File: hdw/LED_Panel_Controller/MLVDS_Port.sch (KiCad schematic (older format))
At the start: 4 parts

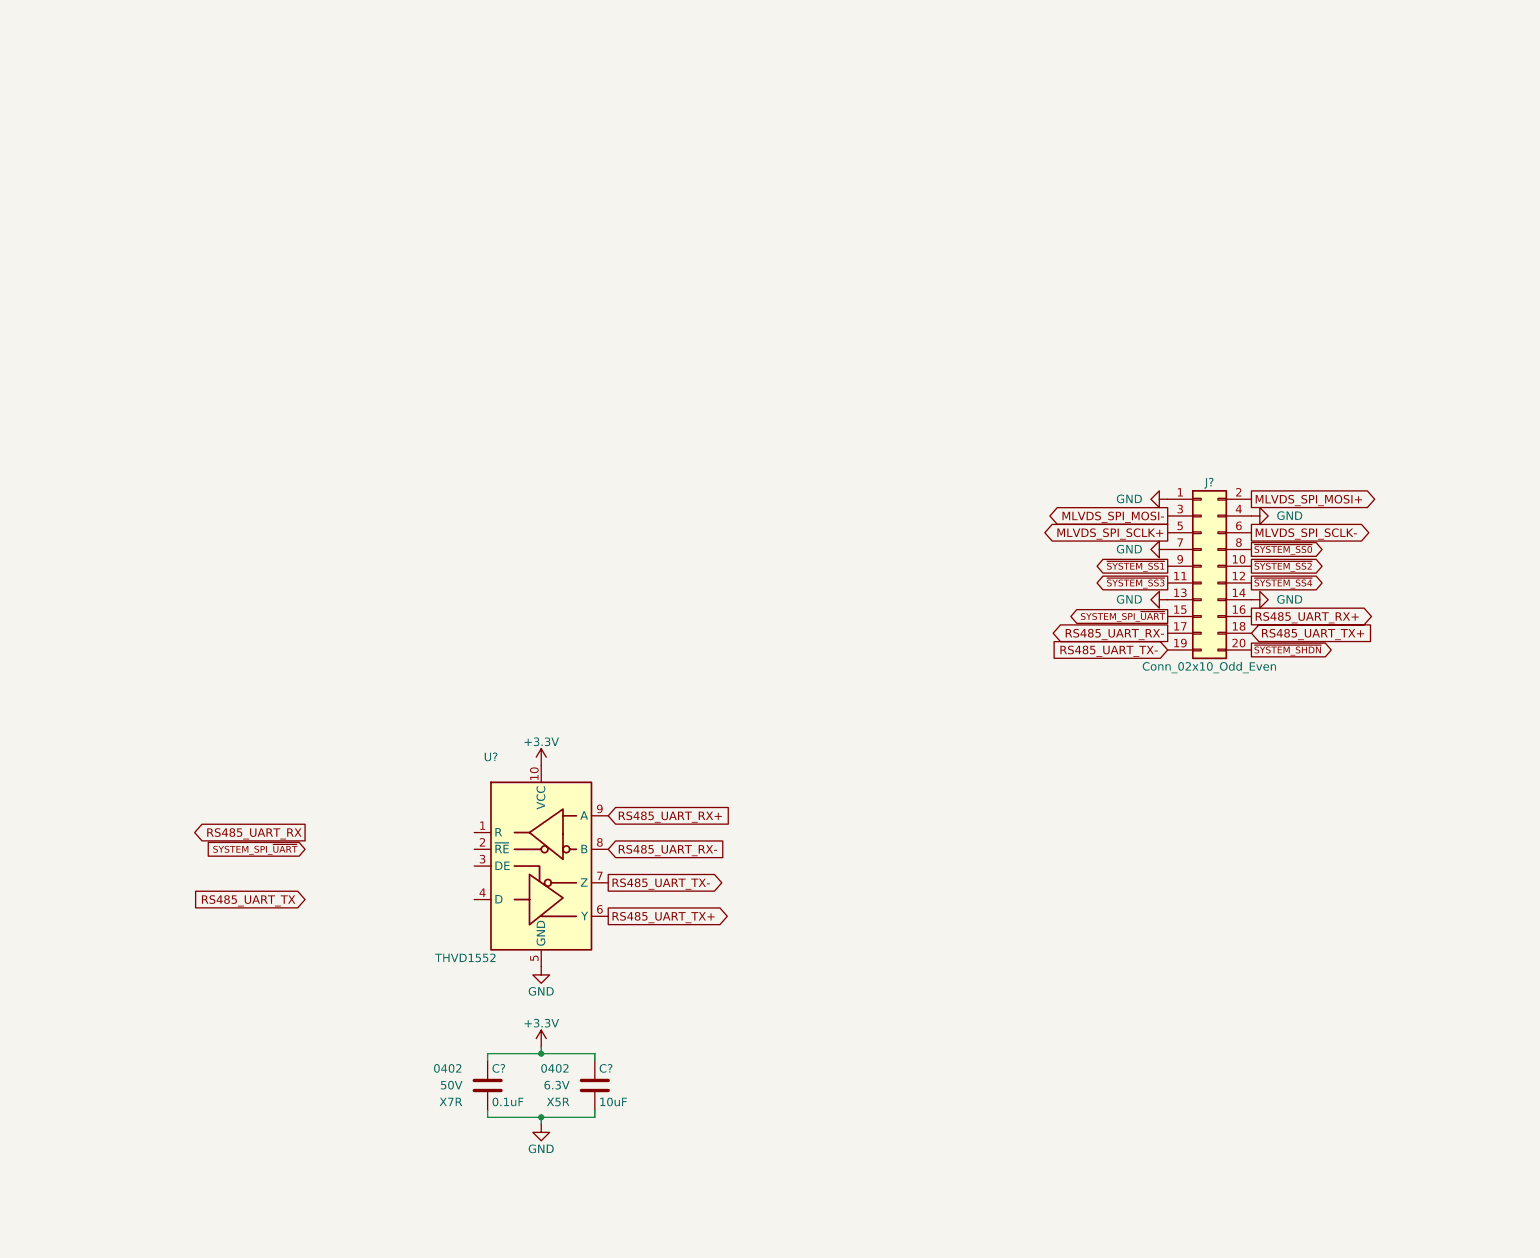
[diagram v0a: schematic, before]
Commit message: reworked schematic to use MLVDS connector instead of wifi module
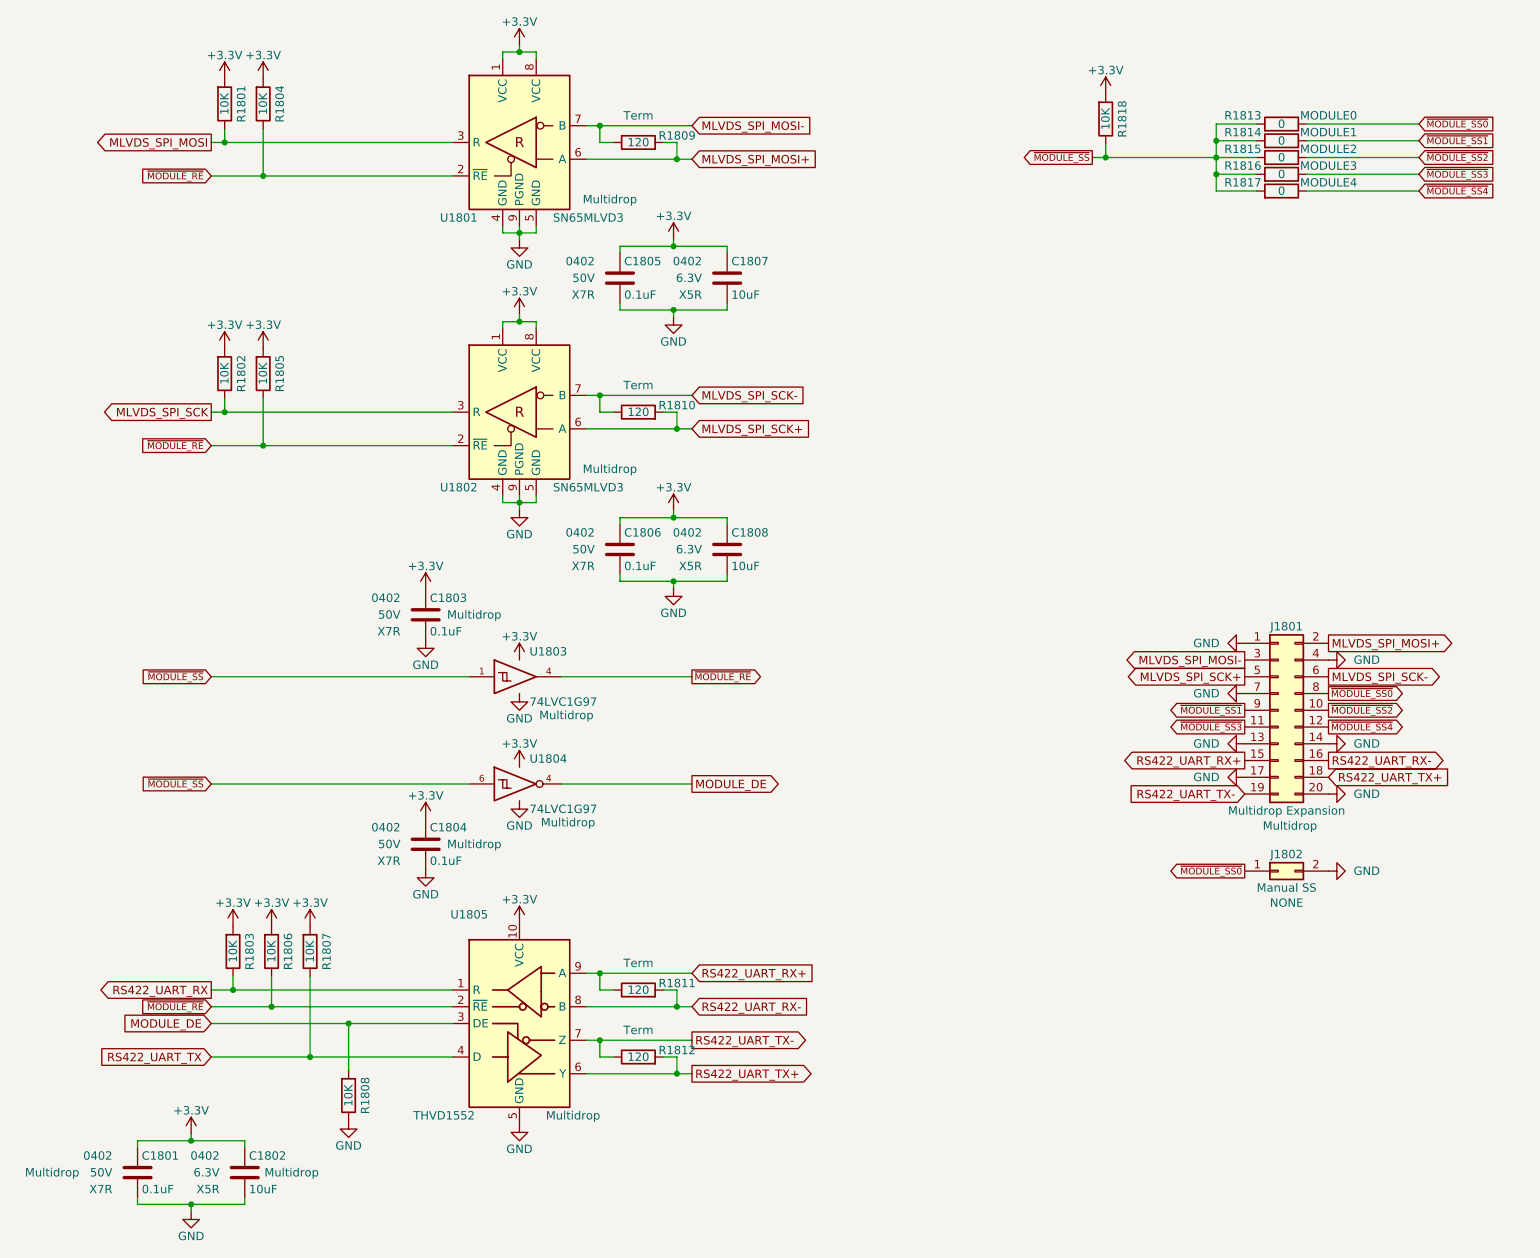
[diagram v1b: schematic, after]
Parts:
- added C1803, C1804, C1805, C1806: 0.1uF, Capacitors_SMD:C_0402, symbol Custom_Library:C_Custom
- added C1807, C1808: 10uF, Capacitors_SMD:C_0402, symbol Custom_Library:C_Custom
- added J1802: Manual SS, symbol Connector_Generic:Conn_02x01
- added R1801, R1802, R1803, R1804, R1805, R1806, R1807, R1808, R1818: 10K, Resistors_SMD:R_0402, symbol Custom_Library:R_Custom
- added R1809, R1810, R1811, R1812: 120, Resistors_SMD:R_0402, symbol Custom_Library:R_Custom
- added R1813, R1814, R1815, R1816, R1817: 0, Resistors_SMD:R_0402, symbol Custom_Library:R_Custom
- added U1801, U1802: SN65MLVD3, Housings_DFN_QFN:DFN-8-1EP_3x3mm_Pitch0.65mm, symbol Custom_Library:SN65MLVD3
- added U1803: 74LVC1G97, Package_TO_SOT_SMD:SOT-363_SC-70-6, symbol Custom_Library:74LVC1G97_Power_BUF
- added U1804: 74LVC1G97, Package_TO_SOT_SMD:SOT-363_SC-70-6, symbol Custom_Library:74LVC1G97_Power_NOT
- C1801, C1802: renamed from C?; Configuration (none) -> Multidrop
- J1801: renamed from J?; value Conn_02x10_Odd_Even -> Multidrop Expansion; footprint (none) -> Connector_IDC:IDC-Header_2x10_P2.54mm_Vertical; Configuration (none) -> Multidrop
- U1805: renamed from U?; Configuration (none) -> Multidrop
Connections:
- net SYSTEM_SPI_~UART is gone; now on net RS422_UART_RX+: J1801.15 (Pin_15)
- net ~SYSTEM_SHDN is gone; now on net GND: J1801.20 (Pin_20)
- net +3V3: now also C1803.1, C1804.1, C1805.1, C1806.1, C1807.1, C1808.1, R1801.1, R1802.1, R1803.1, R1804.1, R1805.1, R1806.1, R1807.1, R1818.1, U1801.1 (VCC), U1801.8 (VCC), U1802.1 (VCC), U1802.8 (VCC), U1803.5 (VCC), U1804.1 (VCC), U1804.5 (VCC)
- net GND: now also J1801.17 (Pin_17), C1803.2, C1804.2, C1805.2, C1806.2, C1807.2, C1808.2, J1802.2 (Pin_2), R1808.2, U1801.4 (GND), U1801.5 (GND), U1801.9 (PGND), U1802.4 (GND), U1802.5 (GND), U1802.9 (PGND), U1803.2 (GND), U1803.3 (GND), U1803.6 (GND), U1804.2 (GND), U1804.3 (GND)
- net MLVDS_SPI_MOSI+: now also R1809.1, U1801.6 (A)
- net MLVDS_SPI_MOSI-: now also R1809.2, U1801.7 (B)
- net RS422_UART_RX: now reaches U1805.1 (R)
- net RS422_UART_RX: now also R1803.2
- net ~MODULE_RE: now reaches U1805.2 (~RE)
- net ~MODULE_RE: now also R1804.2, R1805.2, R1806.2, U1801.2 (~RE), U1802.2 (~RE), U1803.4
- net MODULE_DE: now reaches U1805.3 (DE)
- net MODULE_DE: now also R1808.1, U1804.4
- net RS422_UART_TX: now reaches U1805.4 (D)
- net RS422_UART_TX: now also R1807.2
- net MLVDS_SPI_SCLK+ renamed MLVDS_SPI_SCK+
- net MLVDS_SPI_SCK+: now also R1810.1, U1802.6 (A)
- net MLVDS_SPI_SCLK- renamed MLVDS_SPI_SCK-
- net MLVDS_SPI_SCK-: now also R1810.2, U1802.7 (B)
- net RS485_UART_RX+ renamed RS422_UART_RX+
- net RS422_UART_RX+: now also R1811.2; no longer J1801.16 (Pin_16)
- net RS485_UART_RX- renamed RS422_UART_RX-
- net RS422_UART_RX-: now also J1801.16 (Pin_16), R1811.1; no longer J1801.17 (Pin_17)
- net RS485_UART_TX+ renamed RS422_UART_TX+
- net RS422_UART_TX+: now also R1812.1
- net RS485_UART_TX- renamed RS422_UART_TX-
- net RS422_UART_TX-: now also R1812.2
- net ~SYSTEM_SS0 renamed ~MODULE_SS0
- net ~MODULE_SS0: now also J1802.1 (Pin_1), R1813.2
- net ~SYSTEM_SS1 renamed ~MODULE_SS1
- net ~MODULE_SS1: now also R1814.2
- net ~SYSTEM_SS2 renamed ~MODULE_SS2
- net ~MODULE_SS2: now also R1815.2
- net ~SYSTEM_SS3 renamed ~MODULE_SS3
- net ~MODULE_SS3: now also R1816.2
- net ~SYSTEM_SS4 renamed ~MODULE_SS4
- net ~MODULE_SS4: now also R1817.2
- new net MLVDS_SPI_MOSI: R1801.2, U1801.3 (R)
- new net MLVDS_SPI_SCK: R1802.2, U1802.3 (R)
- new net ~MODULE_SS: R1813.1, R1814.1, R1815.1, R1816.1, R1817.1, R1818.2, U1803.1, U1804.6
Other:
- moved on the sheet: C1801, C1802, J1801, U1805

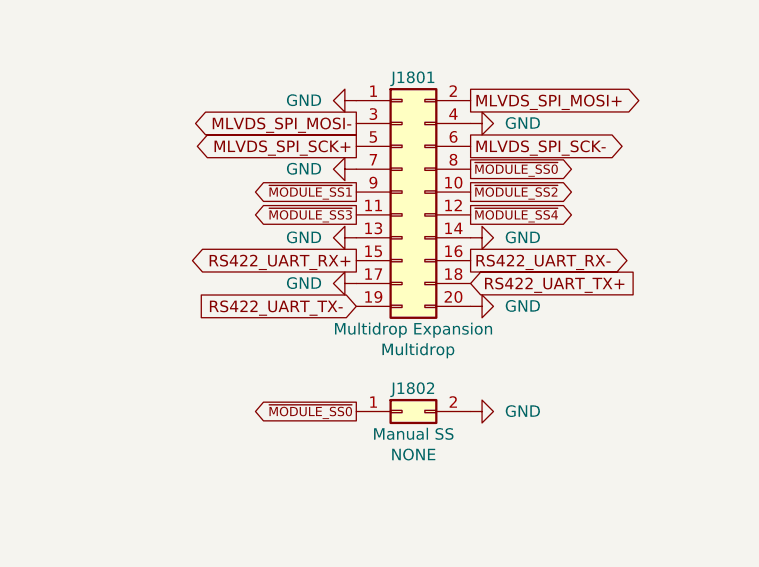
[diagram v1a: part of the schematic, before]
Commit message: started PCB grouping for multidrop expansion port
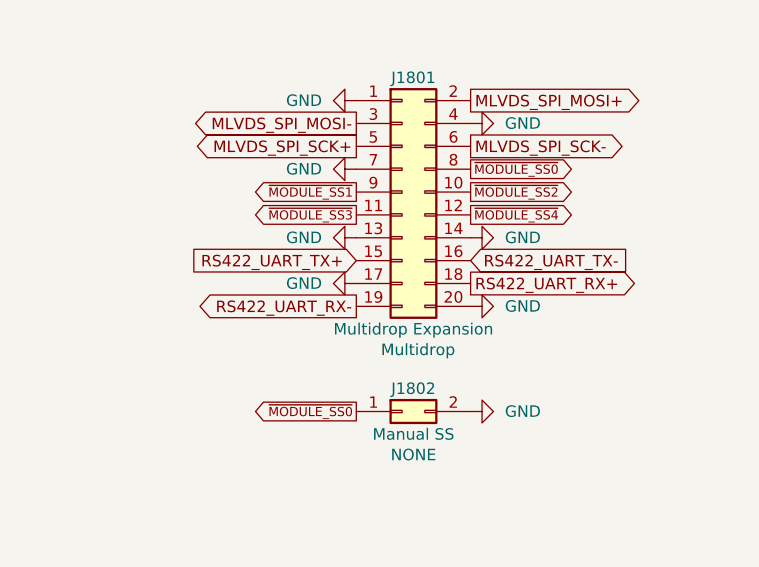
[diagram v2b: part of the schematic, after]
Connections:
- net RS422_UART_RX+: now also J1801.18 (Pin_18); no longer J1801.15 (Pin_15)
- net RS422_UART_RX-: now also J1801.19 (Pin_19); no longer J1801.16 (Pin_16)
- net RS422_UART_TX+: now also J1801.15 (Pin_15); no longer J1801.18 (Pin_18)
- net RS422_UART_TX-: now also J1801.16 (Pin_16); no longer J1801.19 (Pin_19)
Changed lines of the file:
@@
 	0    1    1    0
 $EndComp
-Text GLabel 8740 4990 2    50   Output ~ 0
-RS422_UART_RX-
-Text GLabel 8240 4990 0    50   Output ~ 0
-RS422_UART_RX+
-Text GLabel 8740 5090 2    50   Input ~ 0
+Text GLabel 8240 4990 0    50   Input ~ 0
 RS422_UART_TX+
 $Comp
@@
 	1    0    0    -1
 $EndComp
-Text GLabel 8240 5190 0    50   Input ~ 0
+Text GLabel 8740 4990 2    50   Input ~ 0
 RS422_UART_TX-
 $Comp
@@
 Wire Wire Line
 	7410 1390 7330 1390
+Text GLabel 8740 5090 2    50   Output ~ 0
+RS422_UART_RX+
+Text GLabel 8240 5190 0    50   Output ~ 0
+RS422_UART_RX-
 $EndSCHEMATC

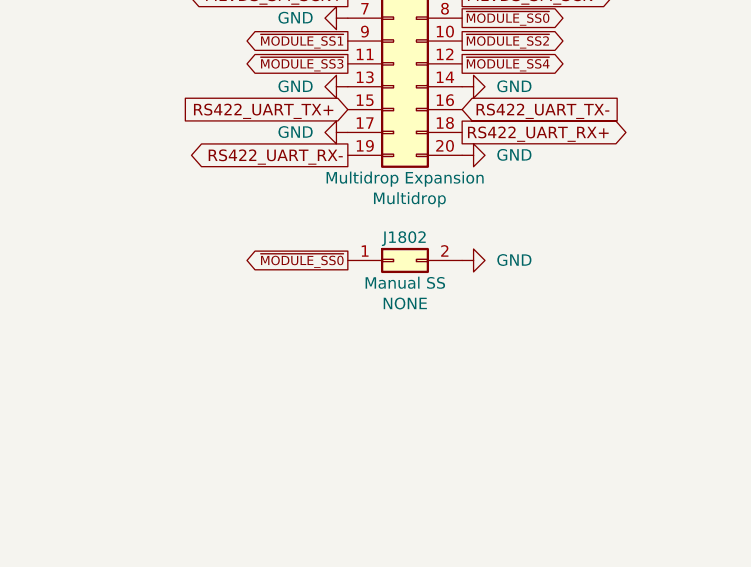
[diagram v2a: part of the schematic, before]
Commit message: arranged more parts on PCB
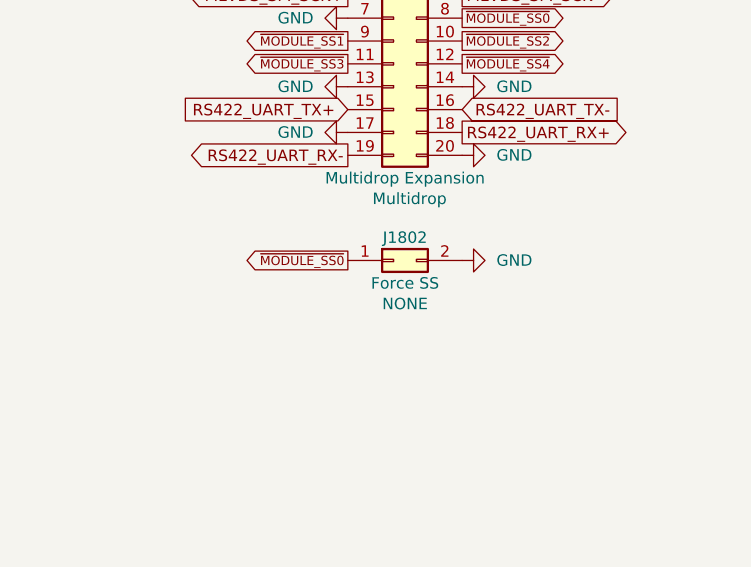
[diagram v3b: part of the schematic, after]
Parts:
- J1802: value Manual SS -> Force SS; footprint (none) -> Connector_PinHeader_2.54mm:PinHeader_1x02_P2.54mm_Vertical
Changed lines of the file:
@@
 P 8440 5650
 F 0 "J1802" H 8490 5750 50  0000 C CNN
-F 1 "Manual SS" H 8490 5550 50  0000 C CNN
-F 2 "" H 8440 5650 50  0001 C CNN
+F 1 "Force SS" H 8490 5550 50  0000 C CNN
+F 2 "Connector_PinHeader_2.54mm:PinHeader_1x02_P2.54mm_Vertical" H 8440 5650 50  0001 C CNN
 F 3 "~" H 8440 5650 50  0001 C CNN
 F 4 "NONE" H 8490 5460 50  0000 C CNN "Configuration"

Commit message: added some more digikey part numbers to schematic
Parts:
- J1801: Digi-Key PN (none) -> 732-2096-ND
- R1809, R1810, R1811, R1812: Digi-Key PN (none) -> RMCF0402FT120RCT-ND
- U1803, U1804: Digi-Key PN (none) -> 1727-1772-1-ND
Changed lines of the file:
@@
 F 3 "~" H 8440 4690 50  0001 C CNN
 F 4 "Multidrop" H 8510 4000 50  0000 C CNN "Configuration"
+F 5 "732-2096-ND" H 8440 4690 50  0001 C CNN "Digi-Key PN"
 	1    8440 4690
 	1    0    0    -1
@@
 F 3 "http://www.ti.com/lit/ds/symlink/sn74lvc1g97.pdf" H 3960 5130 50  0001 C CNN
 F 4 "Multidrop" H 4200 4900 50  0000 C CNN "Configuration"
+F 5 "1727-1772-1-ND" H 3910 5130 50  0001 C CNN "Digi-Key PN"
 	1    3910 5130
 	1    0    0    -1
@@
 F 6 "1/16W" V 4920 6760 50  0001 C CNN "Wattage"
 F 7 "Term" V 4460 6850 50  0000 R CNN "Configuration"
+F 8 "RMCF0402FT120RCT-ND" H 4620 6760 50  0001 C CNN "Digi-Key PN"
 	1    4620 6760
 	0    1    1    0
@@
 F 6 "1/16W" V 4920 6360 50  0001 C CNN "Wattage"
 F 7 "Term" V 4460 6450 50  0000 R CNN "Configuration"
+F 8 "RMCF0402FT120RCT-ND" H 4620 6360 50  0001 C CNN "Digi-Key PN"
 	1    4620 6360
 	0    1    1    0
@@
 F 6 "1/16W" V 4920 1300 50  0001 C CNN "Wattage"
 F 7 "Term" V 4460 1390 50  0000 R CNN "Configuration"
+F 8 "RMCF0402FT120RCT-ND" H 4620 1300 50  0001 C CNN "Digi-Key PN"
 	1    4620 1300
 	0    1    1    0
@@
 F 6 "1/16W" V 4920 2910 50  0001 C CNN "Wattage"
 F 7 "Term" V 4460 3000 50  0000 R CNN "Configuration"
+F 8 "RMCF0402FT120RCT-ND" H 4620 2910 50  0001 C CNN "Digi-Key PN"
 	1    4620 2910
 	0    1    1    0
@@
 F 3 "http://www.ti.com/lit/ds/symlink/sn74lvc1g97.pdf" H 3960 4490 50  0001 C CNN
 F 4 "Multidrop" H 4190 4260 50  0000 C CNN "Configuration"
+F 5 "1727-1772-1-ND" H 3910 4490 50  0001 C CNN "Digi-Key PN"
 	1    3910 4490
 	1    0    0    -1

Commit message: added BOMs, some consolidation
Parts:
- C1801, C1803, C1804, C1805, C1806: Digi-Key PN 490-10701-1-ND -> 490-10698-1-ND
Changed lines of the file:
@@
 F 5 "50V" H 1480 7450 50  0000 R CNN "Voltage"
 F 6 "X7R" H 1480 7350 50  0000 R CNN "Dielectric"
-F 7 "490-10701-1-ND" H -2280 570 50  0001 C CNN "Digi-Key PN"
+F 7 "490-10698-1-ND" H -2280 570 50  0001 C CNN "Digi-Key PN"
 F 8 "Multidrop" H 1120 7450 50  0000 C CNN "Configuration"
 	1    1630 7450
@@
 F 5 "50V" H 4360 2110 50  0000 R CNN "Voltage"
 F 6 "X7R" H 4360 2010 50  0000 R CNN "Dielectric"
-F 7 "490-10701-1-ND" H 600 -4770 50  0001 C CNN "Digi-Key PN"
+F 7 "490-10698-1-ND" H 600 -4770 50  0001 C CNN "Digi-Key PN"
 	1    4510 2110
 	1    0    0    -1
@@
 F 5 "50V" H 4360 3730 50  0000 R CNN "Voltage"
 F 6 "X7R" H 4360 3630 50  0000 R CNN "Dielectric"
-F 7 "490-10701-1-ND" H 600 -3150 50  0001 C CNN "Digi-Key PN"
+F 7 "490-10698-1-ND" H 600 -3150 50  0001 C CNN "Digi-Key PN"
 	1    4510 3730
 	1    0    0    -1
@@
 F 5 "50V" H 3200 5490 50  0000 R CNN "Voltage"
 F 6 "X7R" H 3200 5390 50  0000 R CNN "Dielectric"
-F 7 "490-10701-1-ND" H -560 -1390 50  0001 C CNN "Digi-Key PN"
+F 7 "490-10698-1-ND" H -560 -1390 50  0001 C CNN "Digi-Key PN"
 F 8 "Multidrop" H 3640 5490 50  0000 C CNN "Configuration"
 	1    3350 5490
@@
 F 5 "50V" H 3200 4120 50  0000 R CNN "Voltage"
 F 6 "X7R" H 3200 4020 50  0000 R CNN "Dielectric"
-F 7 "490-10701-1-ND" H -560 -2760 50  0001 C CNN "Digi-Key PN"
+F 7 "490-10698-1-ND" H -560 -2760 50  0001 C CNN "Digi-Key PN"
 F 8 "Multidrop" H 3640 4120 50  0000 C CNN "Configuration"
 	1    3350 4120
